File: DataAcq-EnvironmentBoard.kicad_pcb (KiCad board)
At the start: 2 copper layers, 73.5 x 63.2 mm, 13 parts, among them J1 CAN Output, J2 CAN Input, U1 SHT45, U2 FS3000-1005, U3 LMT87DCK, U4 Daughterboard Connector

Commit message: initial layout/routing
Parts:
- added MH1: M.3, MountingHole:MountingHole_3mm, F.Cu at (136.8, 72.5)
- added MH2: M.3, MountingHole:MountingHole_3mm, F.Cu at (137.0, 120.0)
- added MH3: M.3, MountingHole:MountingHole_3mm, F.Cu at (185.8, 72.5)
- added MH4: M.3, MountingHole:MountingHole_3mm, F.Cu at (185.8, 120.0)
- J1, J2: moved to B.Cu
- moved J2 34.8 mm to (157.0, 77.0), turned to 0 degrees
- moved J1 34.1 mm to (165.8, 115.5), turned to 180 degrees
- moved C2 23.2 mm to (157.8, 84.3), turned to 90 degrees
- moved C1 19.7 mm to (161.0, 85.0)
- moved C6 15.2 mm to (179.2, 106.0)
- moved C5 15.2 mm to (150.2, 103.8), turned to 90 degrees
- moved C4 14.6 mm to (161.5, 90.8), turned to 90 degrees
- moved C3 14.2 mm to (160.5, 96.5), turned to 180 degrees
- moved U2 9.46 mm to (161.5, 90.8), turned to -90 degrees
- moved U1 7.57 mm to (167.3, 104.0)
- moved R1 7.34 mm to (175.1, 106.0)
- moved U3 5.40 mm to (153.1, 103.8)
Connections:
- net Net-(U2-TP1) renamed /AFLW_TP1
- net Net-(U2-TP2) renamed /AFLW_TP2
- net Net-(U2-VCM) renamed /AFLW_VCM
- net Net-(U2-VREG) renamed /AFLW_VREG
- net Net-(U3-OUT) renamed /TEMP_OUT
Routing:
- net /CAN_L: track 0.00 -> 57.2 mm, vias 0 -> 1
- net /CAN_H: track 0.00 -> 51.5 mm, vias 0 -> 2
- net VDDA: track 0.00 -> 37.9 mm, vias 0 -> 2
- net /TEMP_OUT: track 0.00 -> 21.0 mm, vias 0 -> 1
- net /I2C2_SCL: track 0.00 -> 18.9 mm, vias 0 -> 1
- net /I2C2_SDA: track 0.00 -> 16.8 mm, vias 0 -> 1
- net /I2C1_SCL: track 0.00 -> 16.5 mm, vias 0 -> 1
- net /I2C1_SDA: track 0.00 -> 15.1 mm, vias 0 -> 1
- net GND: track 0.00 -> 11.9 mm, vias 0 -> 4
- net +3.3V: track 0.00 -> 11.6 mm, vias 0 -> 5
- net /PA1(ADC): track 0.00 -> 10.7 mm
- net GNDA: track 0.00 -> 9.06 mm, vias 0 -> 4
- net /AFLW_VCM: track 0.00 -> 3.65 mm, vias 0 -> 1
- net /AFLW_TP2: track 0.00 -> 2.87 mm, vias 0 -> 1
- net /AFLW_VREG: track 0.00 -> 2.66 mm, vias 0 -> 1
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- added copper zone on In2.Cu, net +3.3V
- added copper zone on F.Cu, net /+12V_In
- added copper zone on B.Cu, net GND
- added copper zone on In1.Cu, net GNDA
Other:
- board size 73.5 x 63.2 mm -> 56.2 x 53 mm
- copper layers 2 -> 4

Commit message: layout again
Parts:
- moved MH4 96.8 mm to (100.6, 74.0)
- moved MH3 95.7 mm to (91.0, 86.0)
- moved MH2 41.8 mm to (110.4, 87.8)
- moved MH1 23.2 mm to (113.6, 72.2)
- moved J1 18.0 mm to (148.4, 110.8), turned to 90 degrees
- moved C3 17.8 mm to (169.2, 81.0), turned to -90 degrees
- moved J2 16.3 mm to (148.4, 90.8), turned to 90 degrees
- moved C6 15.6 mm to (164.8, 100.0), turned to -90 degrees
- moved R1 14.0 mm to (162.4, 100.0), turned to 90 degrees
- moved U1 12.9 mm to (162.7, 92.0), turned to 0 degrees
- moved C4 10.9 mm to (163.4, 80.1), turned to 180 degrees
- moved U2 10.9 mm to (163.4, 80.1), turned to 0 degrees
- moved C5 9.73 mm to (159.8, 105.6)
- moved U3 9.61 mm to (162.6, 105.2), turned to 0 degrees
- moved C1 5.65 mm to (157.7, 80.5), turned to 90 degrees
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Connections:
- net /+12V_In renamed +12V_In
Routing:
- net +3.3V: track 11.6 -> 40.5 mm, vias 5 -> 3
- net GNDA: track 9.06 -> 33.9 mm, vias 4 -> 3
- net /TEMP_OUT: track 21.0 -> 4.02 mm
- net /PA1(ADC): track 10.7 -> 18.2 mm, vias 0 -> 2
- net /I2C1_SCL: track 16.5 -> 23.7 mm
- net /I2C2_SDA: track 16.8 -> 23.7 mm
- net +12V_In: track 0.00 -> 6.42 mm, vias 0 -> 1
- net /I2C1_SDA: track 15.1 -> 21.3 mm
- net /I2C2_SCL: track 18.9 -> 23.6 mm
- net VDDA: track 37.9 -> 33.4 mm
- net /CAN_H: track 51.5 -> 53.3 mm, vias 2 -> 0
- net GND: track 11.9 -> 10.6 mm, vias 4 -> 5
- removed copper zone on In2.Cu, net +3.3V
- removed copper zone on In1.Cu, net GNDA
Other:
- board size 56.2 x 53 mm -> 42 x 50.2 mm
- copper layers 4 -> 2

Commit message: test points
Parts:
- added D1: 12V, LED_SMD:LED_0805_2012Metric, B.Cu at (166.4, 112.8)
- added D2: 3.3V, LED_SMD:LED_0805_2012Metric, B.Cu at (171.0, 89.6)
- added R2: 22.1k, Resistor_SMD:R_0805_2012Metric, B.Cu at (162.3, 112.8)
- added R3: 2.2k, Resistor_SMD:R_0805_2012Metric, B.Cu at (167.4, 89.6)
- added TP1: TestPoint, Connector_PinHeader_2.54mm:PinHeader_1x01_P2.54mm_Vertical, B.Cu at (158.2, 112.8)
- added TP2: TestPoint, Connector_PinHeader_2.54mm:PinHeader_1x01_P2.54mm_Vertical, B.Cu at (158.2, 116.6)
- added TP4: TestPoint, Connector_PinHeader_2.54mm:PinHeader_1x01_P2.54mm_Vertical, B.Cu at (171.2, 92.6)
- added TP5: TestPoint, Connector_PinHeader_2.54mm:PinHeader_1x01_P2.54mm_Vertical, B.Cu at (167.4, 92.6)
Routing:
- net GNDPWR: track 0.00 -> 34.1 mm, vias 0 -> 1
- net +3.3V: track 40.5 -> 48.2 mm
- net +12V: track 0.00 -> 3.18 mm
- net Net-(D1-A): track 0.00 -> 2.26 mm
- net Net-(D2-A): track 0.00 -> 1.78 mm
- net +12V_In: track 6.42 -> 7.42 mm
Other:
- board text added: "12V"
- board text added: "3.3V"
- board text added: "GND"
- board text added: "GNDPWR"

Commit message: part numbers smh
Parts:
- R1: value 800 -> 1k
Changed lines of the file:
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@@
 			)
 		)
+		(property "P/N" "C0805C104M5RACTU"
+			(at 0 0 90)
+			(unlocked yes)
+			(layer "F.Fab")
+			(hide yes)
+			(effects
+				(font
+					(size 1 1)
+					(thickness 0.15)
+				)
+			)
+		)
 		(property ki_fp_filters "C_*")
 		(sheetname "Root")
@@
 			)
 		)
+		(property "P/N" "C0805C104M5RACTU"
+			(at 0 0 -90)
+			(unlocked yes)
+			(layer "F.Fab")
+			(hide yes)
+			(effects
+				(font
+					(size 1 1)
+					(thickness 0.15)
+				)
+			)
+		)
 		(property ki_fp_filters "C_*")
 		(sheetname "Root")
@@
 			)
 		)
+		(property "P/N" "C0805C104M5RACTU"
+			(at 0 0 90)
+			(unlocked yes)
+			(layer "F.Fab")
+			(hide yes)
+			(effects
+				(font
+					(size 1 1)
+					(thickness 0.15)
+				)
+			)
+		)
 		(property ki_fp_filters "C_*")
 		(sheetname "Root")
@@
 			)
 		)
+		(property "P/N" "C0805C105K5PACTU"
+			(at 0 0 180)
+			(unlocked yes)
+			(layer "F.Fab")
+			(hide yes)
+			(effects
+				(font
+					(size 1 1)
+					(thickness 0.15)
+				)
+			)
+		)
 		(property ki_fp_filters "C_*")
 		(sheetname "Root")
@@
 			)
 		)
-		(property "Value" "800"
+		(property "Value" "1k"
 			(at 0 1.65 90)
 			(layer "F.Fab")
@@
 			)
 		)
+		(property "P/N" "CRCW08051K00FKEAC"
+			(at 0 0 90)
+			(unlocked yes)
+			(layer "F.Fab")
+			(hide yes)
+			(effects
+				(font
+					(size 1 1)
+					(thickness 0.15)
+				)
+			)
+		)
 		(property ki_fp_filters "R_*")
 		(sheetname "Root")
@@
 			)
 		)
+		(property "P/N" "C0805C104M5RACTU"
+			(at 0 0 180)
+			(unlocked yes)
+			(layer "F.Fab")
+			(hide yes)
+			(effects
+				(font
+					(size 1 1)
+					(thickness 0.15)
+				)
+			)
+		)
 		(property ki_fp_filters "C_*")
 		(sheetname "Root")
@@
 			)
 		)
+		(property "P/N" "C0805C105K5PACTU"
+			(at 0 0 -90)
+			(unlocked yes)
+			(layer "F.Fab")
+			(hide yes)
+			(effects
+				(font
+					(size 1 1)
+					(thickness 0.15)
+				)
+			)
+		)
 		(property ki_fp_filters "C_*")
 		(sheetname "Root")
@@
 			)
 		)
+		(property "P/N" "436500244"
+			(at 0 0 90)
+			(unlocked yes)
+			(layer "B.Fab")
+			(hide yes)
+			(effects
+				(font
+					(size 1 1)
+					(thickness 0.15)
+				)
+				(justify mirror)
+			)
+		)
 		(property ki_fp_filters "Connector*:*_1x??_*")
 		(sheetname "Root")
@@
 			)
 		)
+		(property "P/N" "SHT45-AD1B-R3 "
+			(at 0 0 0)
+			(unlocked yes)
+			(layer "B.Fab")
+			(hide yes)
+			(effects
+				(font
+					(size 1 1)
+					(thickness 0.15)
+				)
+				(justify mirror)
+			)
+		)
 		(property ki_fp_filters "Sensirion?DFN*1.5x1.5mm*P0.8mm*SHT4x*")
 		(sheetname "Root")
@@
 			)
 		)
+		(property "P/N" "FS3000-1005"
+			(at 0 0 0)
+			(unlocked yes)
+			(layer "B.Fab")
+			(hide yes)
+			(effects
+				(font
+					(size 1 1)
+					(thickness 0.15)
+				)
+				(justify mirror)
+			)
+		)
 		(sheetname "Root")
 		(sheetfile "DataAcq-EnvironmentBoard.kicad_sch")
@@
 			)
 		)
+		(property "P/N" "436500244"
+			(at 0 0 90)
+			(unlocked yes)
+			(layer "B.Fab")
+			(hide yes)
+			(effects
+				(font
+					(size 1 1)
+					(thickness 0.15)
+				)
+				(justify mirror)
+			)
+		)
 		(property ki_fp_filters "Connector*:*_1x??_*")
 		(sheetname "Root")
@@
 					(thickness 0.15)
 				)
+				(justify mirror)
+			)
+		)
+		(property "P/N" "LMT87QDCKRQ1"
+			(at 0 0 0)
+			(unlocked yes)
+			(layer "B.Fab")
+			(hide yes)
+			(effects
+				(font
+					(size 1 1)
+					(thickness 0.15)
+				)

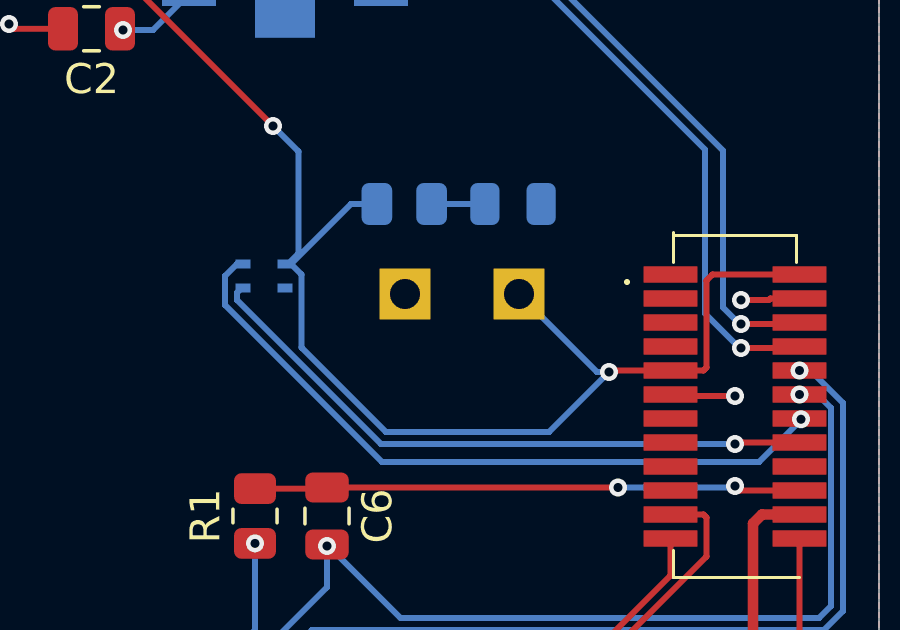
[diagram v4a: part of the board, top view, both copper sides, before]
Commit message: fix ground pad
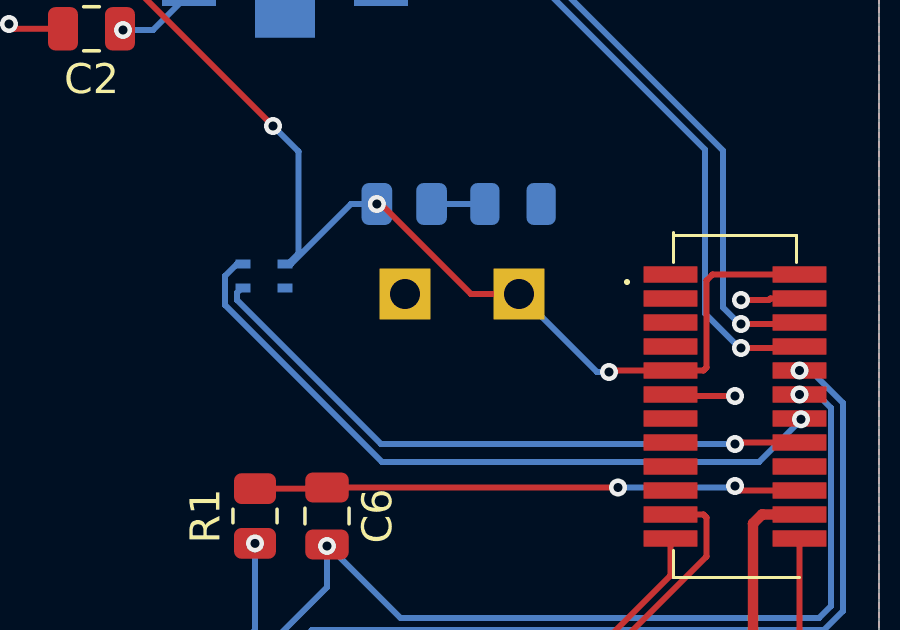
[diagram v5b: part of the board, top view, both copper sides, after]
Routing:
- net +3.3V: track 48.2 -> 39.2 mm, vias 3 -> 4
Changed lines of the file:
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@@
+	)
+	(segment
+		(start 166.4625 89.5375)
+		(end 166.4625 89.6)
+		(width 0.2)
+		(layer "F.Cu")
+		(net 1)
+	)
+	(segment
+		(start 169.6 92.6)
+		(end 166.5 89.5)
+		(width 0.2)
+		(layer "F.Cu")
+		(net 1)
 	)
 	(segment
@@
 	)
 	(segment
+		(start 171.2 92.6)
+		(end 169.6 92.6)
+		(width 0.2)
+		(layer "F.Cu")
+		(net 1)
+	)
+	(segment
 		(start 177.45 92.15)
 		(end 177.45 95.05)
@@
 	)
 	(segment
+		(start 166.5 89.5)
+		(end 166.4625 89.5375)
+		(width 0.2)
+		(layer "F.Cu")
+		(net 1)
+	)
+	(segment
 		(start 177.45 95.05)
 		(end 177.35 95.15)
@@
 	)
 	(via
+		(at 166.4625 89.6)
+		(size 0.6)
+		(drill 0.3)
+		(layers "F.Cu" "B.Cu")
+		(net 1)
+	)
+	(via
 		(at 174.2 95.2)
 		(size 0.6)
@@
 	)
 	(segment
-		(start 172.2 97.2)
-		(end 174.2 95.2)
-		(width 0.2)
-		(layer "B.Cu")
-		(net 1)
-	)
-	(segment
-		(start 163.6 91.6)
-		(end 163.95 91.95)
-		(width 0.2)
-		(layer "B.Cu")
-		(net 1)
-	)
-	(segment
 		(start 163.85 91.25)
 		(end 163.5 91.6)
@@
 	)
 	(segment
-		(start 163.95 94.384314)
-		(end 166.765686 97.2)
-		(width 0.2)
-		(layer "B.Cu")
-		(net 1)
-	)
-	(segment
 		(start 163.4 91.6)
 		(end 163.6 91.6)
@@
 		(width 0.2)
 		(layer "B.Cu")
-		(net 1)
-	)
-	(segment
-		(start 163.95 91.95)
-		(end 163.95 94.384314)
-		(width 0.2)
-		(layer "B.Cu")
-		(net 1)
-	)
-	(segment
-		(start 166.765686 97.2)
-		(end 172.2 97.2)
-		(width 0.2)
-		(layer "B.Cu")

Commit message: rework traces
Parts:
- R2, R3: moved to F.Cu
- moved D1 35.4 mm to (178.4, 79.5)
- moved R2 35.3 mm to (174.0, 79.5)
- moved TP2 27.3 mm to (155.0, 89.5), turned to 180 degrees
- moved TP4 16.2 mm to (155.0, 93.5), turned to -90 degrees
- moved TP5 13.3 mm to (155.0, 97.5), turned to -90 degrees
- moved TP1 11.7 mm to (155.0, 101.5), turned to 180 degrees
- moved D2 10.7 mm to (178.5, 82.0)
- moved R3 10.0 mm to (173.9, 82.0)
- moved U1 3.94 mm to (164.5, 95.5), turned to 90 degrees
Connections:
- R2 pad 1: +12V -> +12V_In
- TP1 pad 1: +12V -> +12V_In
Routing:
- net +3.3V: track 39.2 -> 60.1 mm, vias 4 -> 2
- net GNDPWR: track 34.1 -> 51.8 mm, vias 1 -> 3
- net /I2C1_SCL: track 23.7 -> 17.9 mm
- net /I2C1_SDA: track 21.3 -> 16.3 mm
- net +12V_In: track 7.42 -> 3.13 mm
- net +12V: track 3.18 -> 0.00 mm
- net Net-(D2-A): track 1.78 -> 2.74 mm, vias 0 -> 1
- net Net-(D1-A): track 2.26 -> 2.59 mm, vias 0 -> 1

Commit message: cap
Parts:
- added C7: 0.1uF, Capacitor_SMD:C_0805_2012Metric, F.Cu at (164.5, 93.0)
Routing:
- net GND: track 10.7 -> 12.8 mm, vias 5 -> 6
- net +3.3V: track 60.1 -> 61.2 mm, vias 2 -> 3
